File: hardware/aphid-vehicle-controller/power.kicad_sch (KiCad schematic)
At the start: 39 parts, among them U2 AMS1117-3.3, U3 LMR33630BDDA

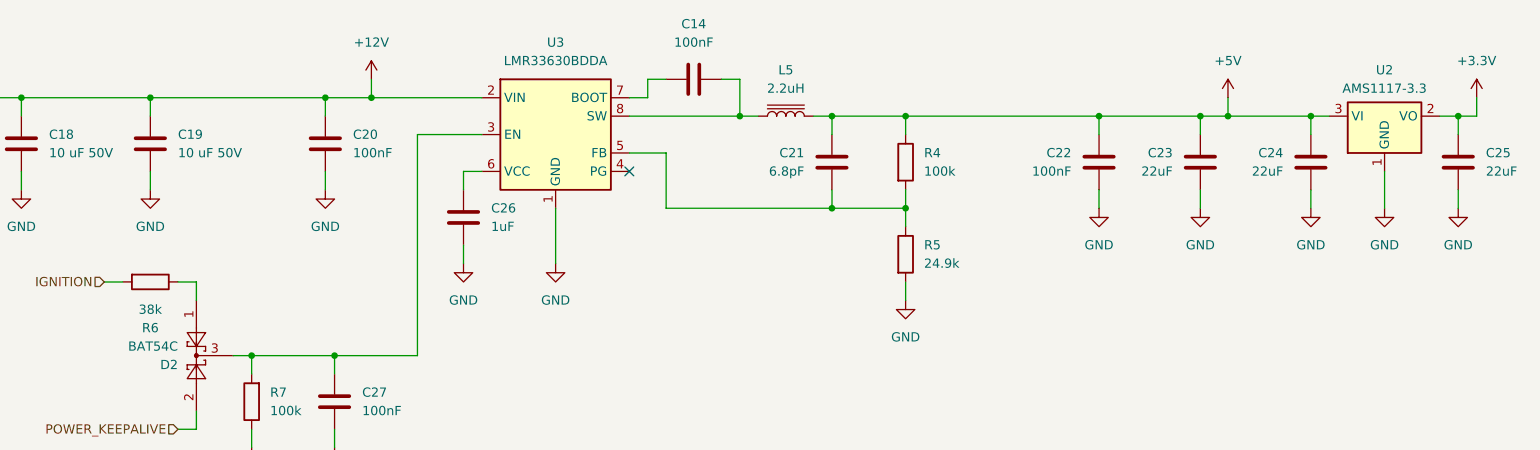
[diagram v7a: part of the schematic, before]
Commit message: Harmonized VC and BMS components
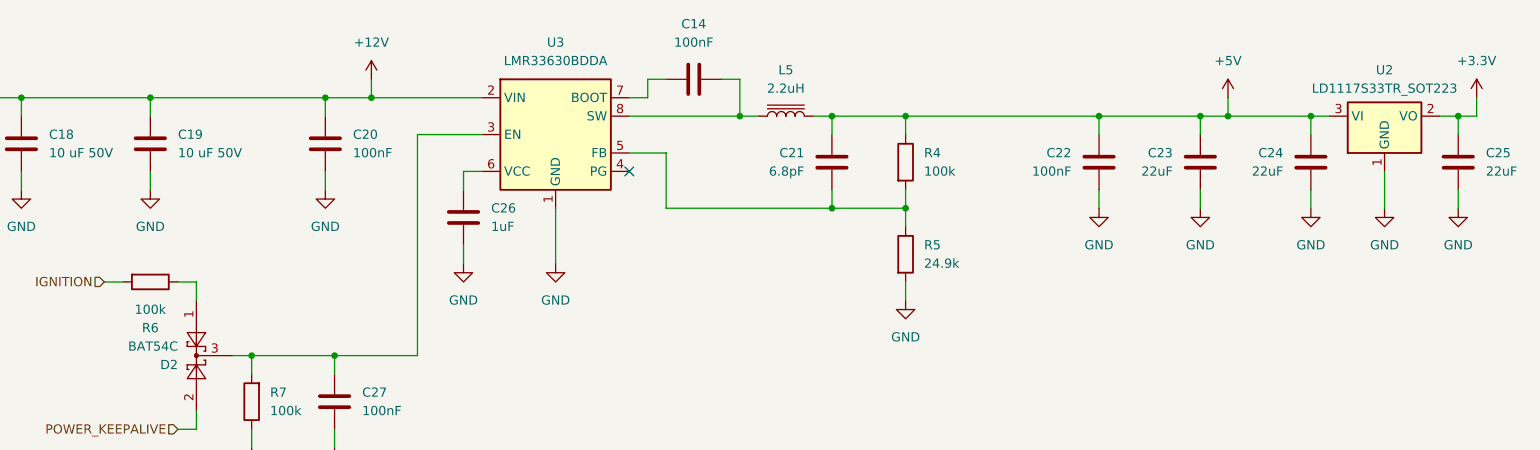
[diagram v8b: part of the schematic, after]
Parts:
- removed U2: AMS1117-3.3, Package_TO_SOT_SMD:SOT-223-3_TabPin2, symbol Regulator_Linear:AMS1117-3.3
- added U2: LD1117S33TR_SOT223, Package_TO_SOT_SMD:SOT-223-3_TabPin2, symbol Regulator_Linear:LD1117S33TR_SOT223
- R6: value 38k -> 100k
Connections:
- net +3.3V: now also U2.2 (VO)
- net +5V: now also U2.3 (VI)
- net GND: now also U2.1 (GND)
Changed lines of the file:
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@@
 			)
 		)
-		(property "Value" "38k"
+		(property "Value" "100k"
 			(at 95.25 63.5 90)
 			(effects
@@
 	)
 	(symbol
+		(lib_id "Regulator_Linear:LD1117S33TR_SOT223")
+		(at 265.43 36.83 0)
+		(unit 1)
+		(exclude_from_sim no)
+		(in_bom yes)
+		(on_board yes)
+		(dnp no)
+		(fields_autoplaced yes)
+		(property "Reference" "U2"
+			(at 265.43 30.48 0)
+			(effects
+				(font
+					(size 1.27 1.27)
+				)
+			)
+		)
+		(property "Value" "LD1117S33TR_SOT223"
+			(at 265.43 33.02 0)
+			(effects
+				(font
+					(size 1.27 1.27)
+				)
+			)
+		)
+		(property "Footprint" "Package_TO_SOT_SMD:SOT-223-3_TabPin2"
+			(at 265.43 31.75 0)
+			(effects
+				(font
+					(size 1.27 1.27)
+				)
+				(hide yes)
+			)
+		)
+		(property "Datasheet" "http://www.st.com/st-web-ui/static/active/en/resource/technical/document/datasheet/CD00000544.pdf"
+			(at 267.97 43.18 0)
+			(effects
+				(font
+					(size 1.27 1.27)
+				)
+				(hide yes)
+			)
+		)
+		(property "Description" "800mA Fixed Low Drop Positive Voltage Regulator, Fixed Output 3.3V, SOT-223"
+			(at 265.43 36.83 0)
+			(effects
+				(font
+					(size 1.27 1.27)
+				)
+				(hide yes)
+			)
+		)
+		(pin "2"
+		)
+		(pin "1"
+		)
+		(pin "3"
+		)
+		(instances
+			(project ""
+				(path "/1bdad060-e59b-443f-afdb-9aa678a43546/98781d90-1f08-466f-be3c-fdb64160be3c"
+					(reference "U2")
+					(unit 1)
+				)
+			)
+		)
+	)
+	(symbol
 		(lib_id "power:PWR_FLAG")
 		(at 242.57 156.21 180)
@@
 					(unit 1)
 				)
-			)
-		)
-	)
-	(symbol
-		(lib_id "Regulator_Linear:AMS1117-3.3")
-		(at 265.43 36.83 0)
-		(unit 1)
-		(exclude_from_sim no)
-		(in_bom yes)
-		(on_board yes)
-		(dnp no)
-		(fields_autoplaced yes)
-		(property "Reference" "U2"
-			(at 265.43 30.48 0)
-			(effects
-				(font
-					(size 1.27 1.27)
-				)
-			)
-		)
-		(property "Value" "AMS1117-3.3"
-			(at 265.43 33.02 0)
-			(effects
-				(font
-					(size 1.27 1.27)
-				)
-			)
-		)
-		(property "Footprint" "Package_TO_SOT_SMD:SOT-223-3_TabPin2"
-			(at 265.43 31.75 0)
-			(effects
-				(font
-					(size 1.27 1.27)
-				)
-				(hide yes)
-			)
-		)
-		(property "Datasheet" "http://www.advanced-monolithic.com/pdf/ds1117.pdf"
-			(at 267.97 43.18 0)
-			(effects
-				(font
-					(size 1.27 1.27)
-				)
-				(hide yes)
-			)
-		)
-		(property "Description" "1A Low Dropout regulator, positive, 3.3V fixed output, SOT-223"
-			(at 265.43 36.83 0)
-			(effects
-				(font
-					(size 1.27 1.27)
-				)
-				(hide yes)
-			)
-		)
-		(pin "3"
-		)
-		(pin "2"
-		)
-		(pin "1"
-		)
-		(instances
-			(project "aphid-vehicle-controller"
-				(path "/1bdad060-e59b-443f-afdb-9aa678a43546/98781d90-1f08-466f-be3c-fdb64160be3c"
-					(reference "U2")
-					(unit 1)
-				)
